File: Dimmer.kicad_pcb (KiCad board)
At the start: 2 copper layers, 156.1 x 68 mm, 57 parts, among them J1 220to12, J11 220v_OUT, J16 Conn_01x06, J2 Prog, J22 SPI, J3 UART0, J4 Conn_01x06, J9 220v_IN, Q1 IRFP460APBF, Q2 IRFP460APBF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

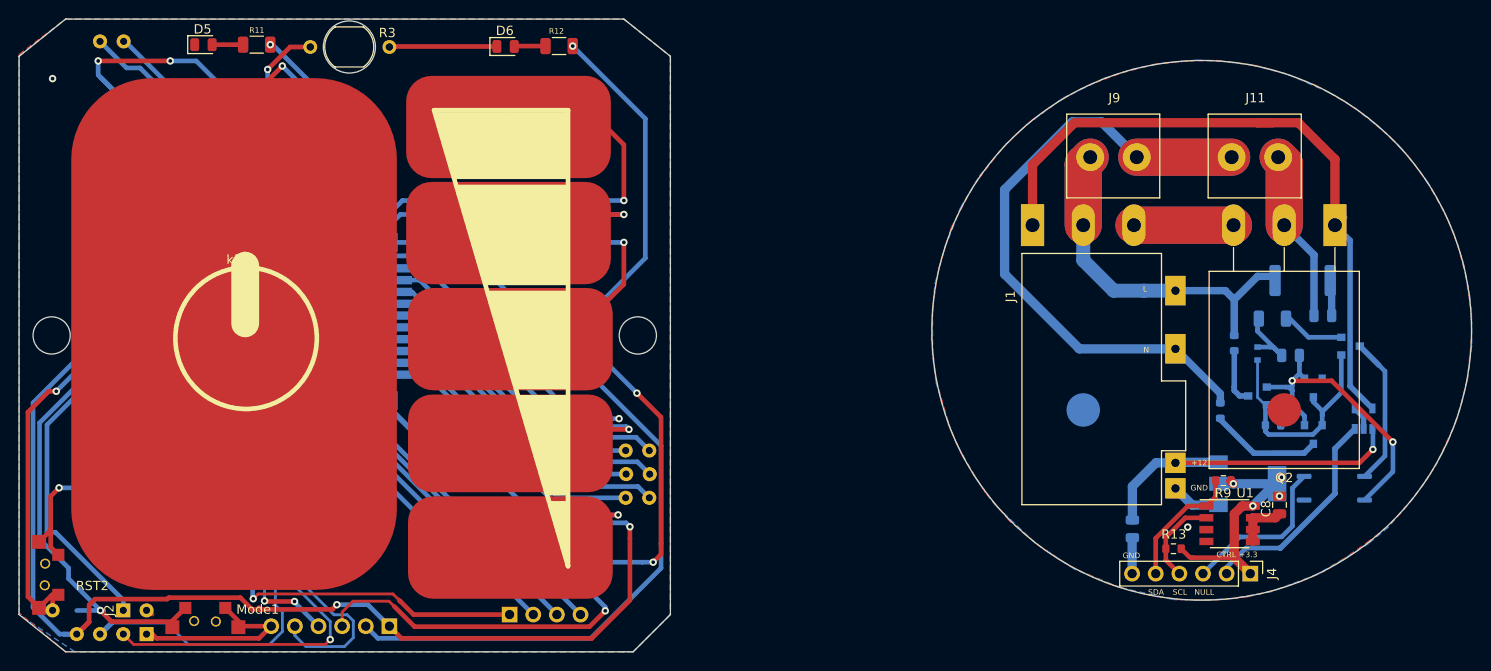
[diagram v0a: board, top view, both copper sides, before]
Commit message: Ordered
Sensor solder mask fix
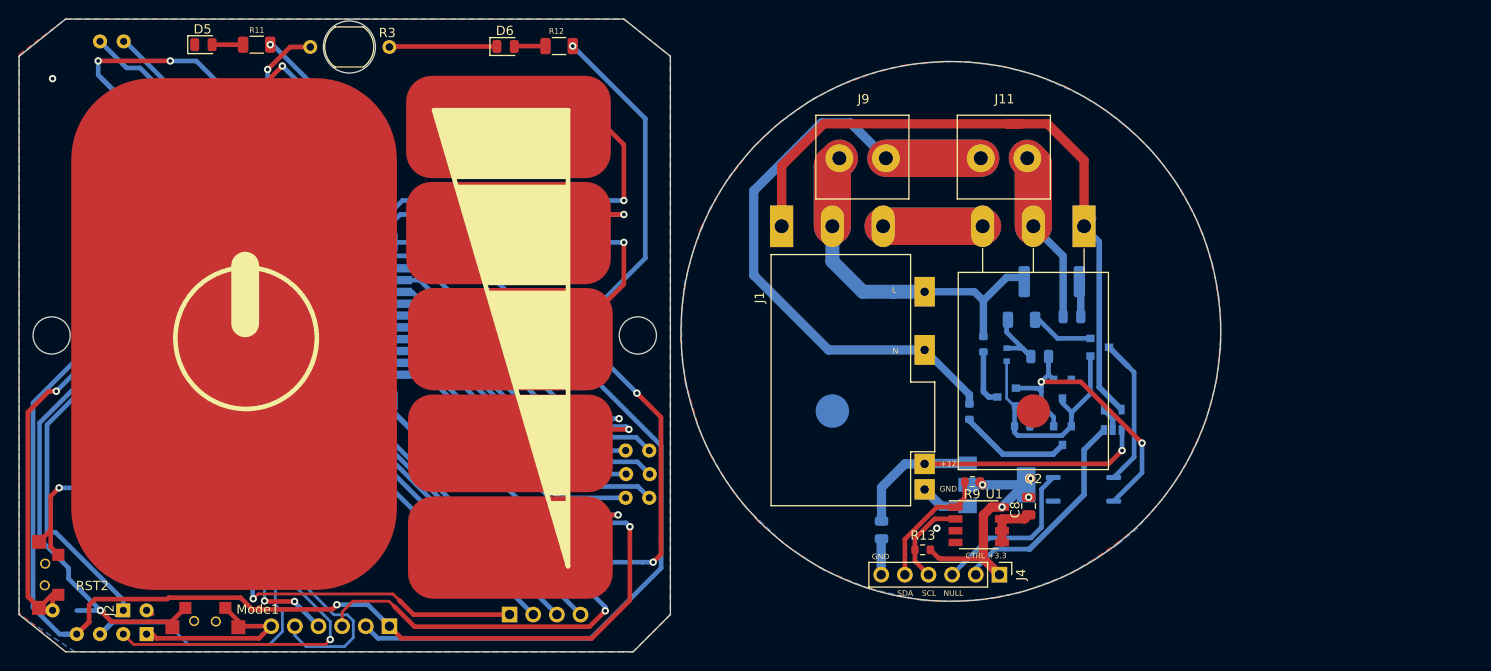
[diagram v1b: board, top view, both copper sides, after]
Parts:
- moved C1 27.0 mm to (193.6, 101.9)
- moved C2 27.0 mm to (190.1, 106.2)
- moved C8 27.0 mm to (188.9, 122.2)
- moved J1 27.0 mm to (161.2, 95.2)
- moved J9 27.0 mm to (176.1, 80.1)
- moved R8 27.0 mm to (188.2, 113.7)
- moved C11 27.0 mm to (173.1, 124.8)
- moved D1 27.0 mm to (186.5, 110.5)
- moved D2 27.0 mm to (192.5, 114.7)
- moved D3 27.0 mm to (192.5, 109.7)
- moved D4 27.0 mm to (186.5, 106.0)
- moved D7 27.0 mm to (197.9, 113.0)
- moved J11 27.0 mm to (191.3, 80.1)
- moved J4 27.0 mm to (185.8, 129.6)
- moved Q1 27.0 mm to (162.4, 92.2)
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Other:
- board size 156.1 x 68 mm -> 129.1 x 68 mm

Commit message: Заменены посадочные места, переразведена нижняя плата
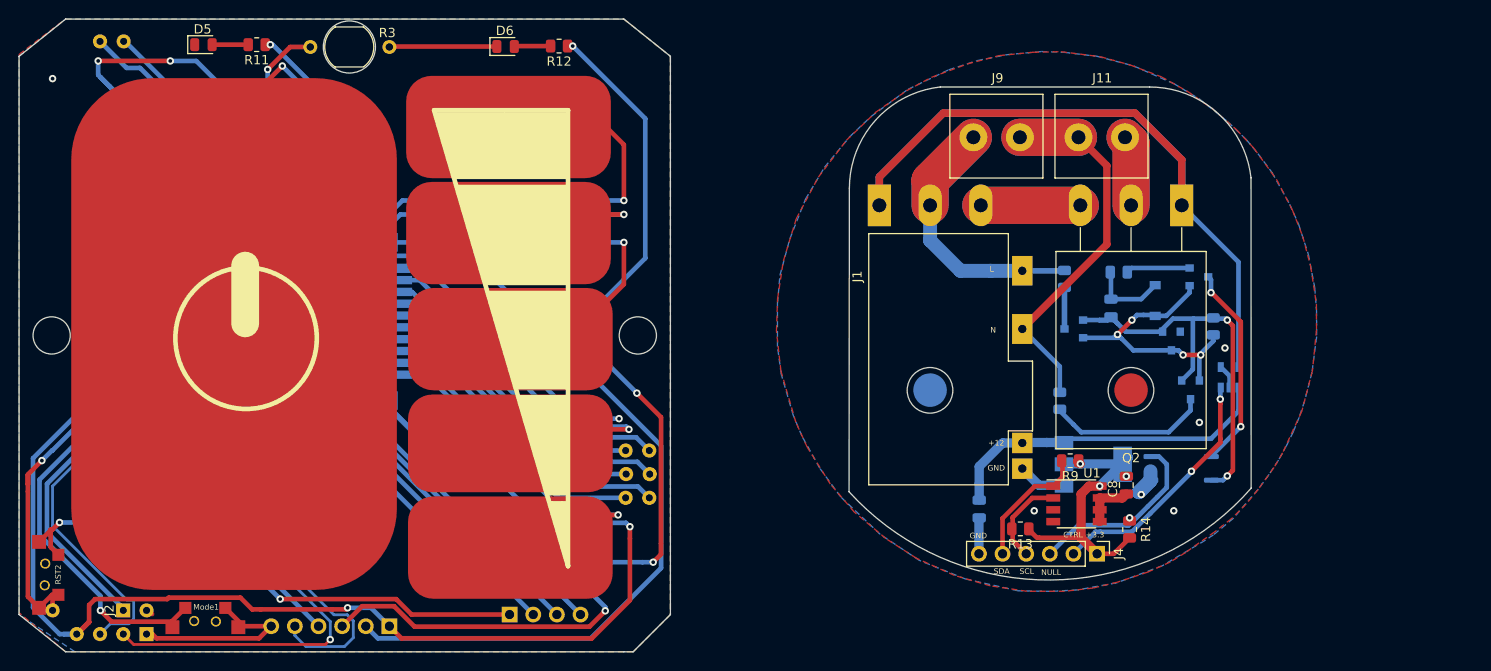
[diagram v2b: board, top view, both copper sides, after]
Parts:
- removed C1: 0.01mk, Capacitor_SMD:C_0805_2012Metric
- removed R7: 220 1W, Resistor_SMD:R_2512_6332Metric
- added R14: 10k, Resistor_SMD:R_0805_2012Metric, F.Cu at (199.8, 124.8)
- C4: footprint Capacitor_SMD:C_1210_3225Metric -> Capacitor_SMD:C_0805_2012Metric
- D4: footprint Diode_SMD:D_SOD-523 -> Diode_SMD:D_SOD-123
- R1, R10, R11, R12: footprint Resistor_SMD:R_1206_3216Metric -> Resistor_SMD:R_0805_2012Metric
- R13, R4, R5, R6, R8, R9: footprint Resistor_SMD:R_0603_1608Metric -> Resistor_SMD:R_0805_2012Metric
- moved R8 23.2 mm to (208.8, 102.9), turned to 90 degrees
- moved D4 17.0 mm to (202.5, 100.2)
- moved D2 14.6 mm to (206.3, 109.8)
- moved J9 14.6 mm to (190.5, 77.9)
- moved D7 13.4 mm to (210.5, 108.4)
- moved Q3 13.1 mm to (207.2, 97.6)
- moved D3 12.8 mm to (204.2, 104.5)
- moved R10 11.6 mm to (198.6, 97.1)
- moved R4 11.2 mm to (192.8, 97.8)
- moved C11 10.7 mm to (183.6, 122.6)
- moved C8 10.7 mm to (199.4, 120.0)
- moved J1 10.7 mm to (171.7, 93.0)
- moved J11 10.7 mm to (201.8, 77.9)
- moved J4 10.7 mm to (196.3, 127.4)
- moved Q1 10.7 mm to (172.9, 89.9)
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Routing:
- net Net-(D7-Pad5): track 73.8 -> 110.6 mm
- net Net-(J1-Pad2): track 77.8 -> 46.8 mm
- net GND: track 154.9 -> 171.5 mm, vias 4 -> 8
- net Net-(J11-Pad1): track 26.0 -> 15.2 mm
- net Net-(C2-Pad2): track 35.9 -> 45.3 mm
- net Net-(J1-Pad1): track 47.0 -> 38.3 mm
- net Mode: track 78.1 -> 72.0 mm
- net Net-(Q3-Pad3): track 16.0 -> 22.1 mm, vias 0 -> 2
- net Net-(D1-Pad2): track 25.4 -> 30.0 mm, vias 0 -> 4
- net Net-(J2-Pad1): track 71.1 -> 66.8 mm
- net Net-(C1-Pad1): track 4.02 -> 0.00 mm
- net Detect_null: track 17.8 -> 21.6 mm, vias 0 -> 1
- net Net-(R2-Pad2): track 78.4 -> 74.9 mm
- net Load_cntrl: track 23.4 -> 26.7 mm, vias 0 -> 2
- net Net-(J3-Pad2): track 48.7 -> 51.9 mm
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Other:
- board size 129.1 x 68 mm -> 132.4 x 68 mm

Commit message: Добавлены С1 и R7
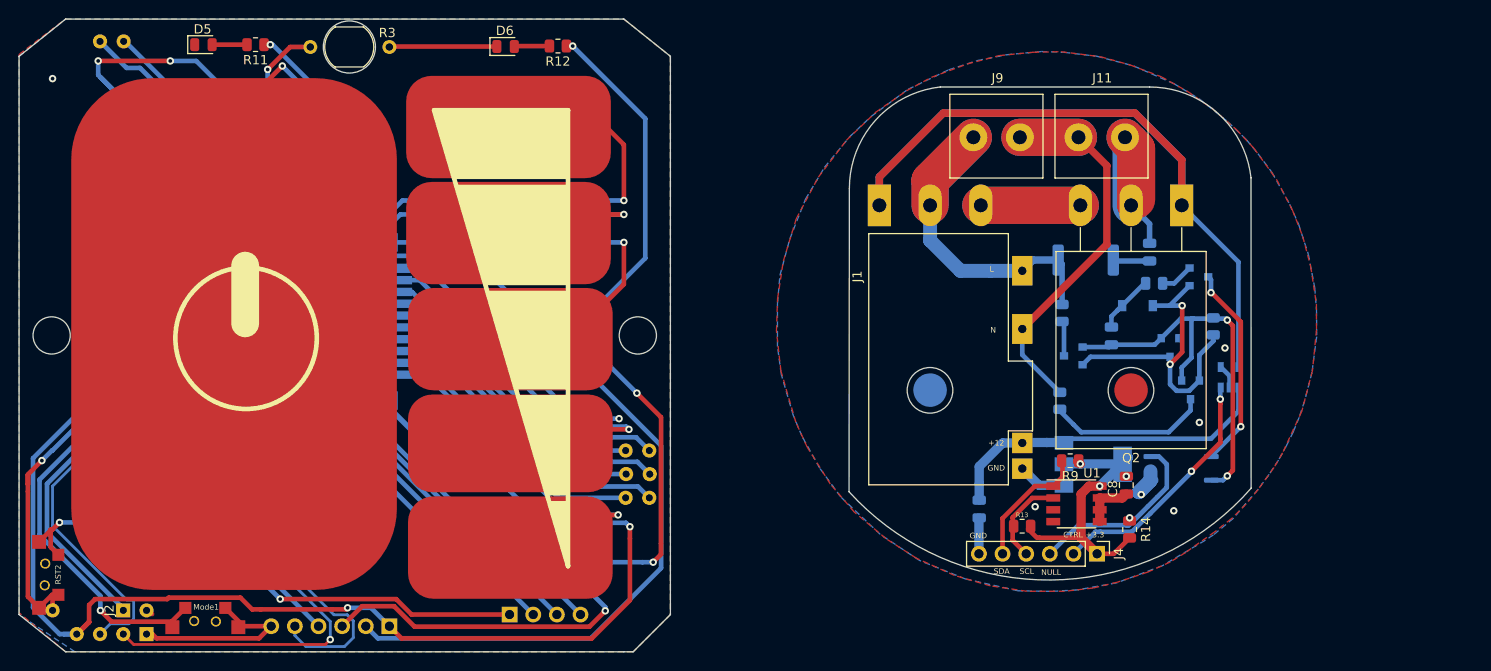
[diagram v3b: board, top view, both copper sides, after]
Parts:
- added C1: 0.1 mk, Capacitor_SMD:C_0805_2012Metric, B.Cu at (201.9, 95.0)
- added R7: 220 1W, Resistor_SMD:R_2512_6332Metric, B.Cu at (195.0, 95.8)
- moved R10 3.98 mm to (202.4, 98.3)
- moved R4 3.67 mm to (192.5, 101.5)
- moved C2 3.00 mm to (197.8, 104.0)
- moved D1 2.90 mm to (193.7, 106.1)
- moved D4 1.98 mm to (200.6, 100.7), turned to 0 degrees
- moved D3 0.72 mm to (204.1, 105.2)
- moved R13 0.35 mm to (188.2, 124.4)
- moved R11 0.12 mm to (105.8, 72.7)
- moved R12 0.12 mm to (138.3, 72.8)
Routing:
- net Net-(C1-Pad2): track 15.2 -> 28.1 mm
- net Net-(D1-Pad2): track 30.0 -> 35.3 mm, vias 4 -> 2
- net Net-(J1-Pad1): track 38.3 -> 43.1 mm
- net Net-(C1-Pad1): track 0.00 -> 3.94 mm
- net Net-(Q3-Pad2): track 6.89 -> 3.58 mm
- net Net-(C2-Pad2): track 45.3 -> 43.1 mm
- net Net-(C2-Pad1): track 8.40 -> 6.97 mm
- net Net-(D1-Pad3): track 4.55 -> 3.78 mm
- net RED: track 103.0 -> 103.6 mm
- net BLUE: track 24.3 -> 24.9 mm
- net +3V3: track 260.9 -> 261.4 mm
- net photo: track 26.1 -> 26.6 mm

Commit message: Замена С1, блок 220-12 поставлен вертикально
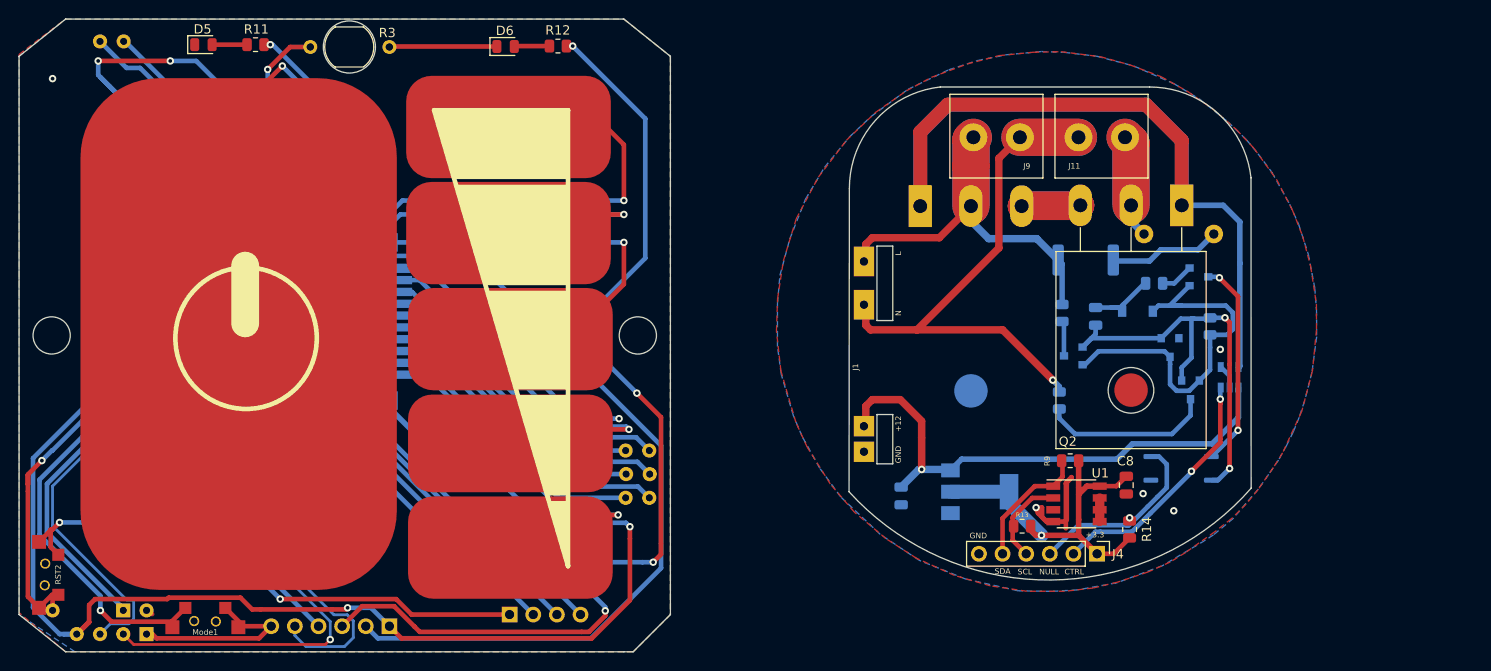
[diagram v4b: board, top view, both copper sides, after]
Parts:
- C1: footprint Capacitor_SMD:C_0805_2012Metric -> Capacitor_THT:C_Rect_L10.0mm_W2.5mm_P7.50mm_MKS4
- moved J1 17.1 mm to (154.7, 91.2)
- moved U22 12.6 mm to (183.7, 120.7)
- moved C11 8.51 mm to (175.2, 121.2)
- moved C1 7.17 mm to (208.8, 93.0), turned to 180 degrees
- moved Q1 4.39 mm to (177.2, 90.0)
- moved C2 2.70 mm to (196.1, 101.8)
- moved D4 0.60 mm to (200.6, 101.3)
- moved R8 0.35 mm to (208.4, 102.9)
- moved R6 0.06 mm to (192.2, 110.9)
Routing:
- net +12V: track 36.9 -> 57.3 mm, vias 0 -> 1
- net Net-(J1-Pad2): track 46.7 -> 64.2 mm, vias 0 -> 1
- net Net-(C1-Pad2): track 28.1 -> 18.8 mm
- net Net-(C1-Pad1): track 3.94 -> 12.0 mm
- net +3V3: track 261.4 -> 268.2 mm, vias 7 -> 5
- net Net-(D1-Pad2): track 35.3 -> 40.5 mm, vias 2 -> 0
- net Net-(J1-Pad1): track 43.1 -> 47.5 mm
- net Net-(D7-Pad5): track 110.6 -> 114.3 mm
- net GND: track 171.5 -> 175.1 mm, vias 8 -> 7
- net Net-(C2-Pad2): track 43.1 -> 45.8 mm
- net Net-(C2-Pad1): track 6.97 -> 8.62 mm
- net Net-(D2-Pad3): track 17.4 -> 18.4 mm
- net null: track 68.0 -> 68.7 mm
- net Net-(Q3-Pad3): track 22.1 -> 22.6 mm
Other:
- outline, holes or cut-outs redrawn

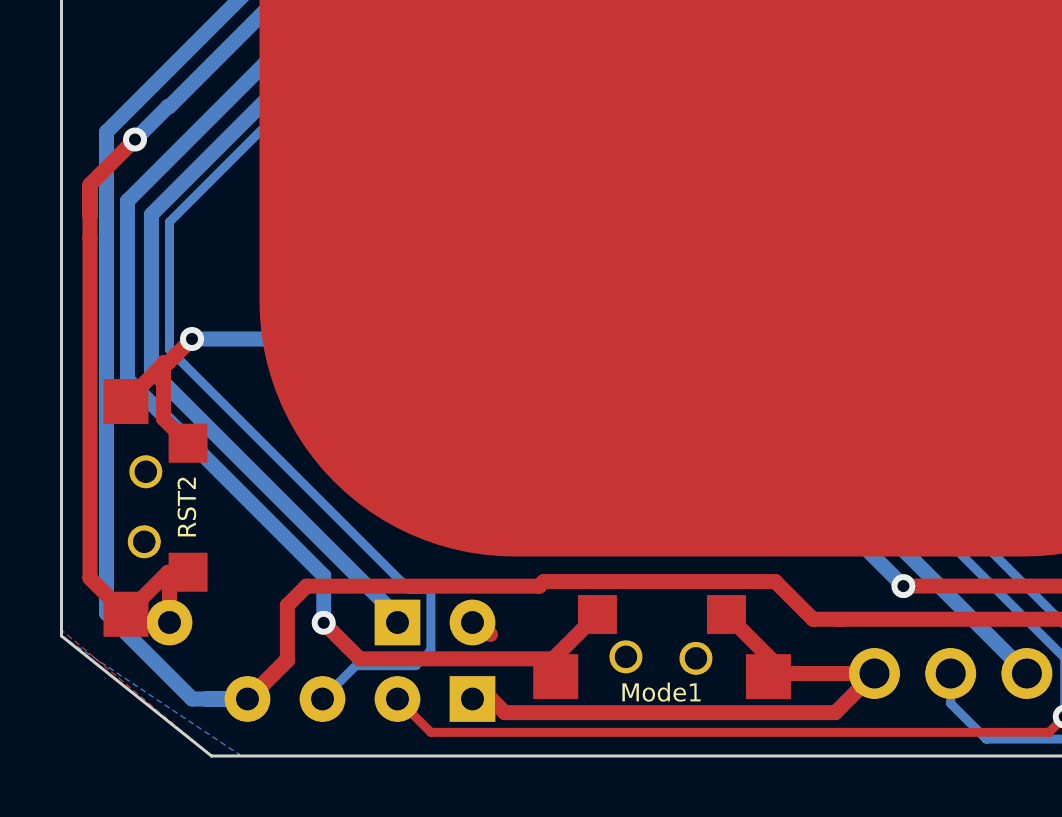
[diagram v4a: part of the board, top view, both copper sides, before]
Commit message: Замена кнопок
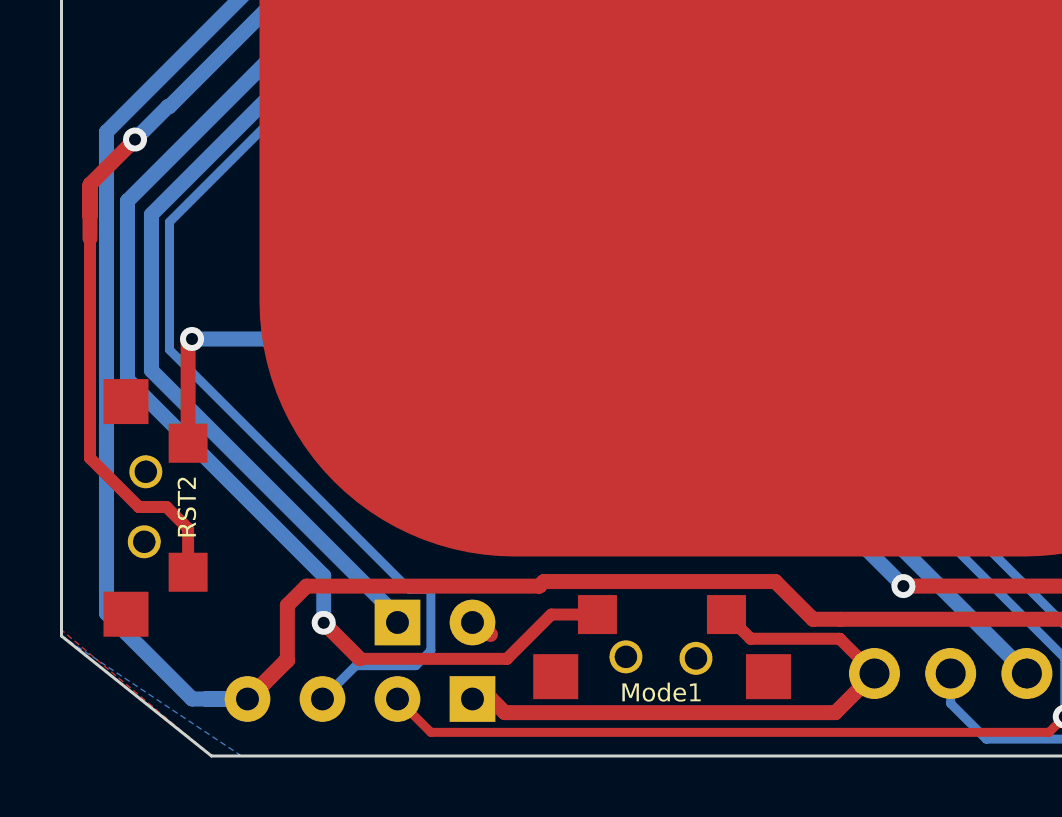
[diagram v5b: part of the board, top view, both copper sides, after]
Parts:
- removed RST1: Rst, SMout:polz_razjem
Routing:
- net Net-(R2-Pad2): track 74.9 -> 70.3 mm
- net GND: track 175.1 -> 172.4 mm
- net Mode: track 72.0 -> 71.2 mm
